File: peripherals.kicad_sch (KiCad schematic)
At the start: 1 part, among them U1 MIMX8MN5DVPIZAA

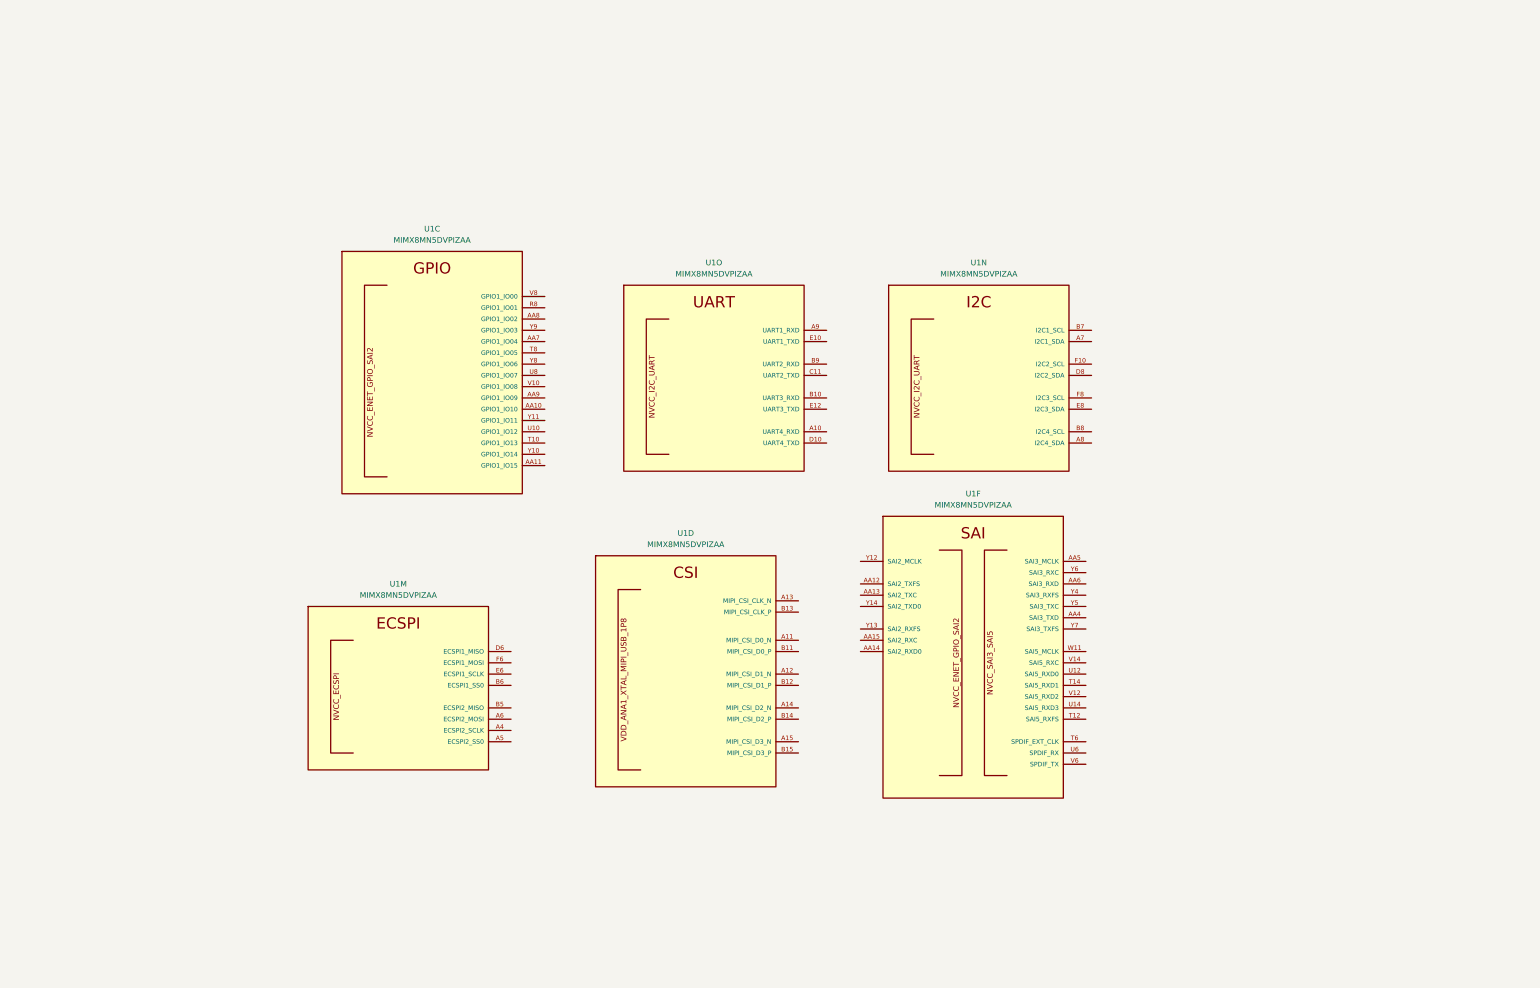
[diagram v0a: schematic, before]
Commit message: move to i.MX8M Mini
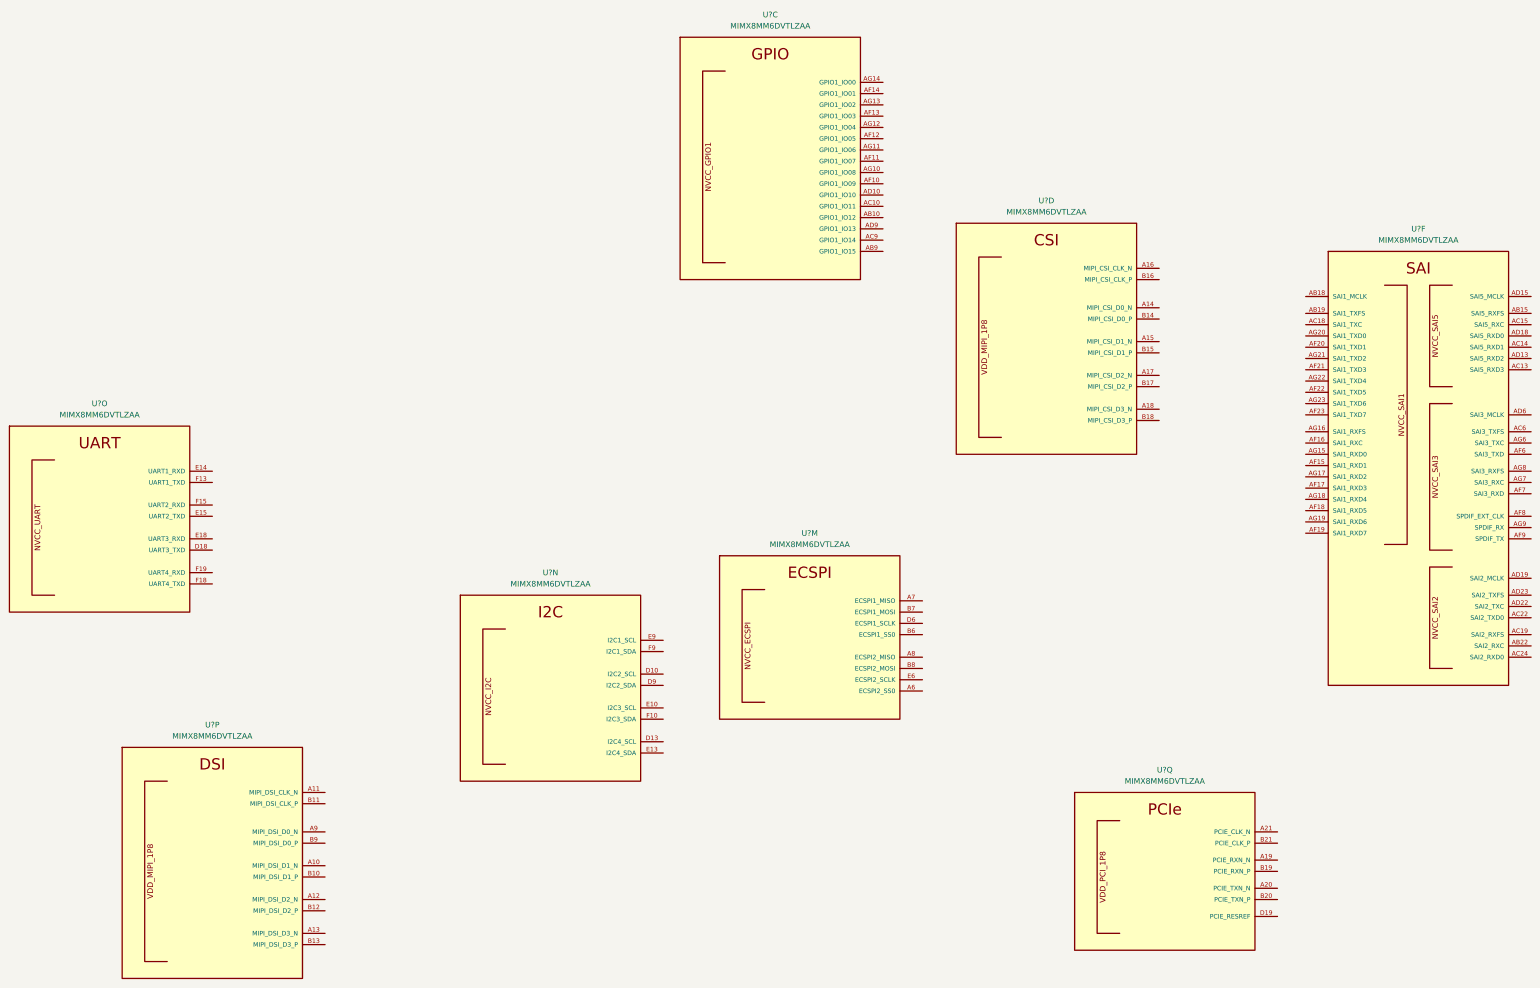
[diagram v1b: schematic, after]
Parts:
- removed U1: MIMX8MN5DVPIZAA, qsbc:SOT1967-1, symbol qsbc:MIMX8MN5DVPIZAA
- added U? (x8): MIMX8MM6DVTLZAA, qsbc:SOT1967-1, symbol qsbc:MIMX8MM6DVTLZAA

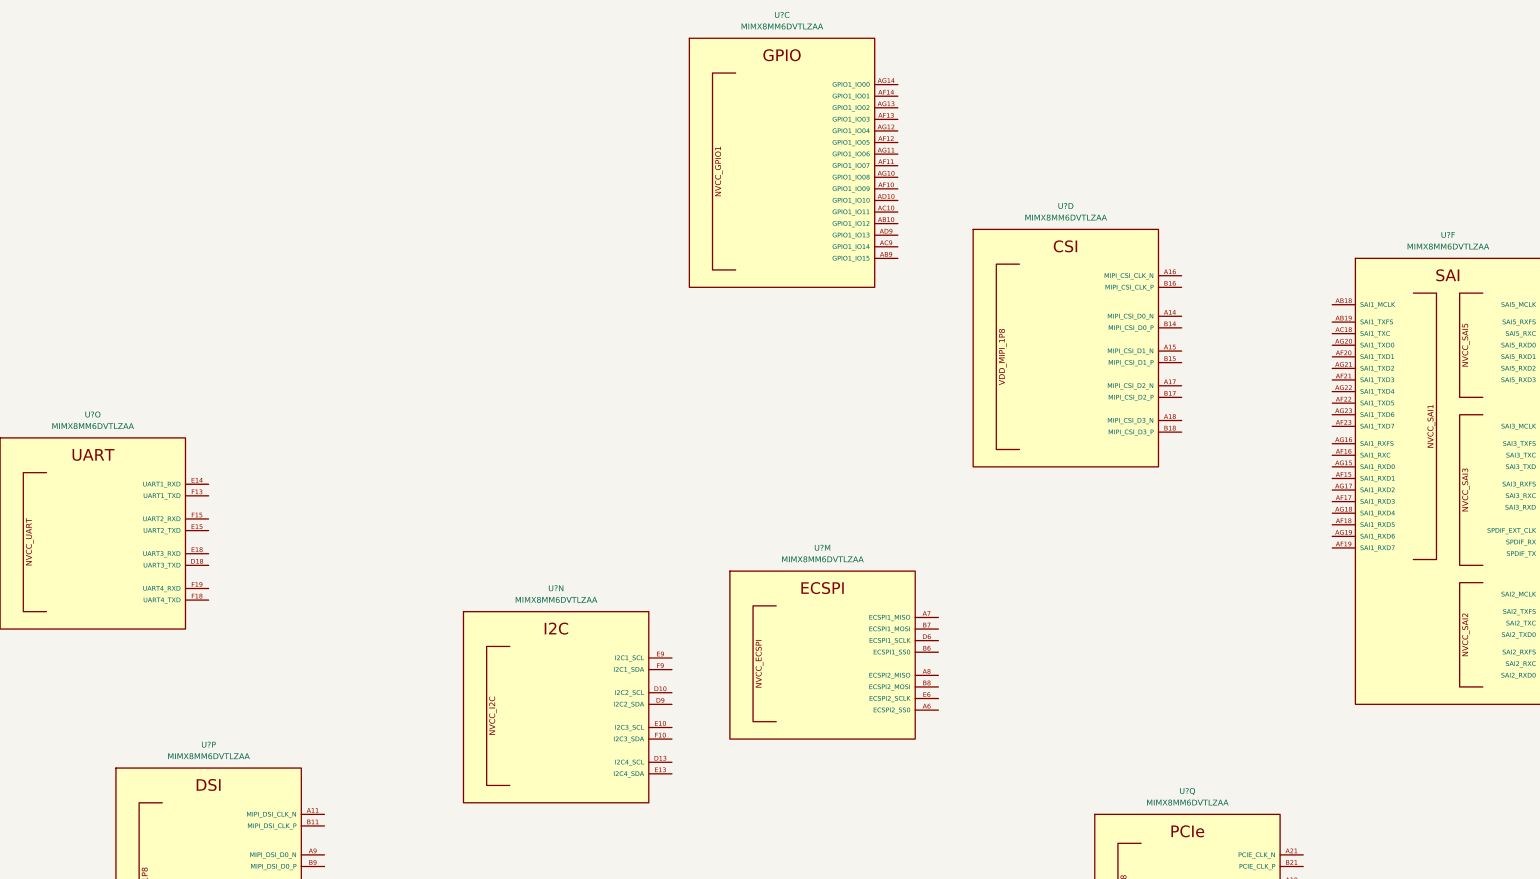
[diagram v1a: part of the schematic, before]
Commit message: ddr sch done
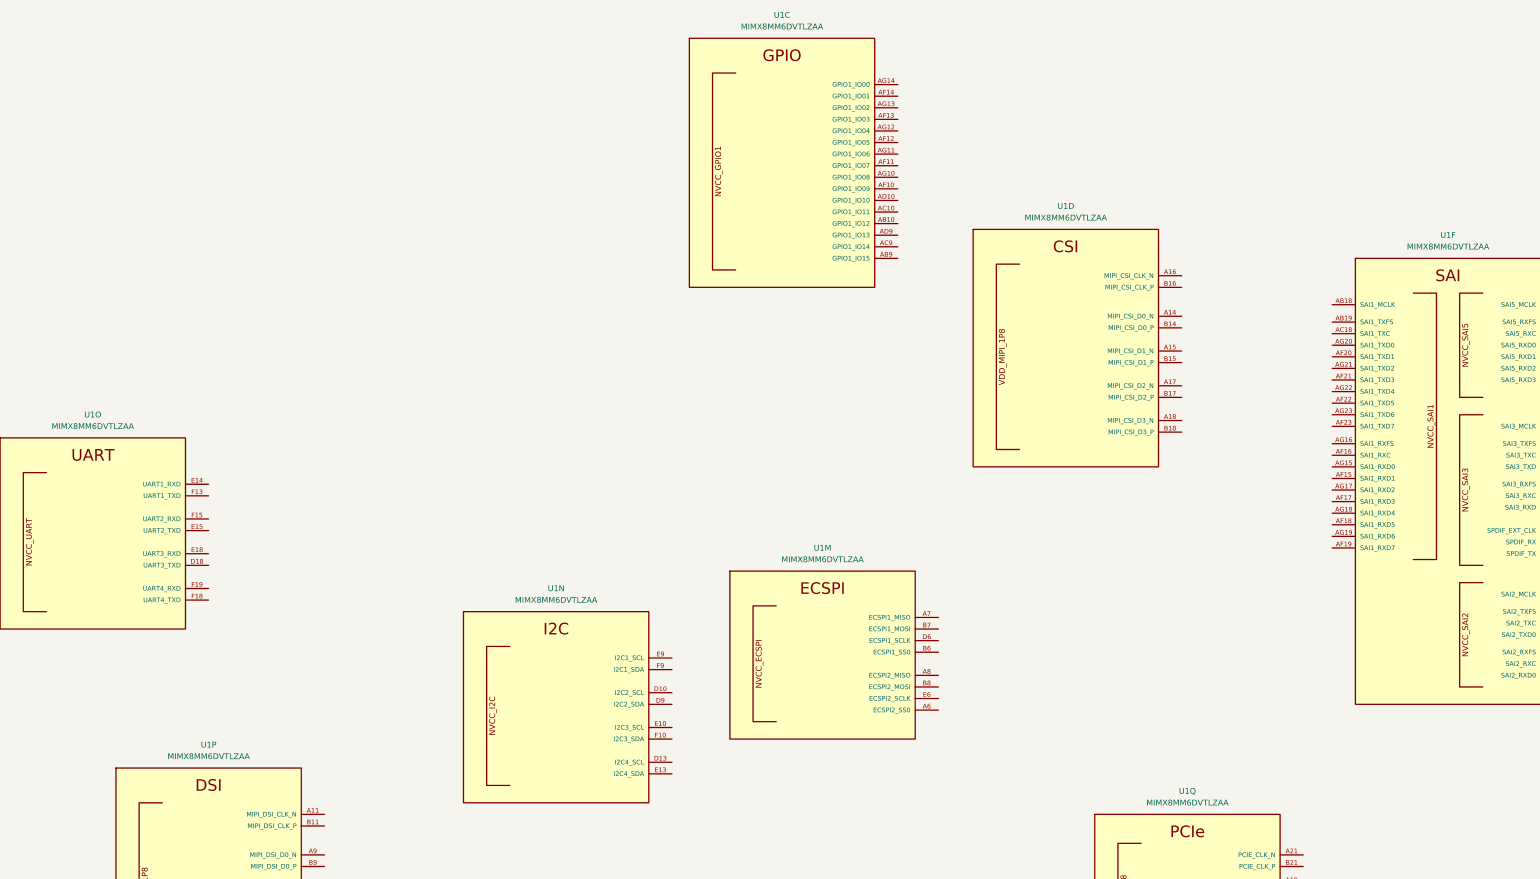
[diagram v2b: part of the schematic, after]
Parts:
- gave numbers to parts that had none: 1
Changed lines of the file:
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@@
   (symbol (lib_id "qsbc:MIMX8MM6DVTLZAA") (at 361.95 91.44 0) (unit 6)
     (in_bom yes) (on_board yes) (fields_autoplaced)
-    (property "Reference" "U?" (id 0) (at 361.95 72.39 0))
+    (property "Reference" "U1" (id 0) (at 361.95 72.39 0))
     (property "Value" "MIMX8MM6DVTLZAA" (id 1) (at 361.95 74.93 0))
     (property "Footprint" "qsbc:SOT1967-1" (id 2) (at 365.76 281.94 0)
@@
   (symbol (lib_id "qsbc:MIMX8MM6DVTLZAA") (at 224.79 160.02 0) (unit 13)
     (in_bom yes) (on_board yes) (fields_autoplaced)
-    (property "Reference" "U?" (id 0) (at 224.79 140.97 0))
+    (property "Reference" "U1" (id 0) (at 224.79 140.97 0))
     (property "Value" "MIMX8MM6DVTLZAA" (id 1) (at 224.79 143.51 0))
     (property "Footprint" "qsbc:SOT1967-1" (id 2) (at 228.6 350.52 0)
@@
   (symbol (lib_id "qsbc:MIMX8MM6DVTLZAA") (at 90.17 203.2 0) (unit 16)
     (in_bom yes) (on_board yes) (fields_autoplaced)
-    (property "Reference" "U?" (id 0) (at 90.17 184.15 0))
+    (property "Reference" "U1" (id 0) (at 90.17 184.15 0))
     (property "Value" "MIMX8MM6DVTLZAA" (id 1) (at 90.17 186.69 0))
     (property "Footprint" "qsbc:SOT1967-1" (id 2) (at 93.98 393.7 0)
@@
   (symbol (lib_id "qsbc:MIMX8MM6DVTLZAA") (at 64.77 130.81 0) (unit 15)
     (in_bom yes) (on_board yes) (fields_autoplaced)
-    (property "Reference" "U?" (id 0) (at 64.77 111.76 0))
+    (property "Reference" "U1" (id 0) (at 64.77 111.76 0))
     (property "Value" "MIMX8MM6DVTLZAA" (id 1) (at 64.77 114.3 0))
     (property "Footprint" "qsbc:SOT1967-1" (id 2) (at 68.58 321.31 0)
@@
   (symbol (lib_id "qsbc:MIMX8MM6DVTLZAA") (at 278.13 85.09 0) (unit 4)
     (in_bom yes) (on_board yes) (fields_autoplaced)
-    (property "Reference" "U?" (id 0) (at 278.13 66.04 0))
+    (property "Reference" "U1" (id 0) (at 278.13 66.04 0))
     (property "Value" "MIMX8MM6DVTLZAA" (id 1) (at 278.13 68.58 0))
     (property "Footprint" "qsbc:SOT1967-1" (id 2) (at 281.94 275.59 0)
@@
   (symbol (lib_id "qsbc:MIMX8MM6DVTLZAA") (at 215.9 43.18 0) (unit 3)
     (in_bom yes) (on_board yes) (fields_autoplaced)
-    (property "Reference" "U?" (id 0) (at 215.9 24.13 0))
+    (property "Reference" "U1" (id 0) (at 215.9 24.13 0))
     (property "Value" "MIMX8MM6DVTLZAA" (id 1) (at 215.9 26.67 0))
     (property "Footprint" "qsbc:SOT1967-1" (id 2) (at 219.71 233.68 0)
@@
   (symbol (lib_id "qsbc:MIMX8MM6DVTLZAA") (at 166.37 168.91 0) (unit 14)
     (in_bom yes) (on_board yes) (fields_autoplaced)
-    (property "Reference" "U?" (id 0) (at 166.37 149.86 0))
+    (property "Reference" "U1" (id 0) (at 166.37 149.86 0))
     (property "Value" "MIMX8MM6DVTLZAA" (id 1) (at 166.37 152.4 0))
     (property "Footprint" "qsbc:SOT1967-1" (id 2) (at 170.18 359.41 0)
@@
   (symbol (lib_id "qsbc:MIMX8MM6DVTLZAA") (at 304.8 213.36 0) (unit 17)
     (in_bom yes) (on_board yes) (fields_autoplaced)
-    (property "Reference" "U?" (id 0) (at 304.8 194.31 0))
+    (property "Reference" "U1" (id 0) (at 304.8 194.31 0))
     (property "Value" "MIMX8MM6DVTLZAA" (id 1) (at 304.8 196.85 0))
     (property "Footprint" "qsbc:SOT1967-1" (id 2) (at 308.61 403.86 0)

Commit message: misc work, usb sch done
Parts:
- removed unit 15 of U1
- removed unit 17 of U1
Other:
- moved on the sheet: U1C, U1D, U1F, U1M, U1N, U1P

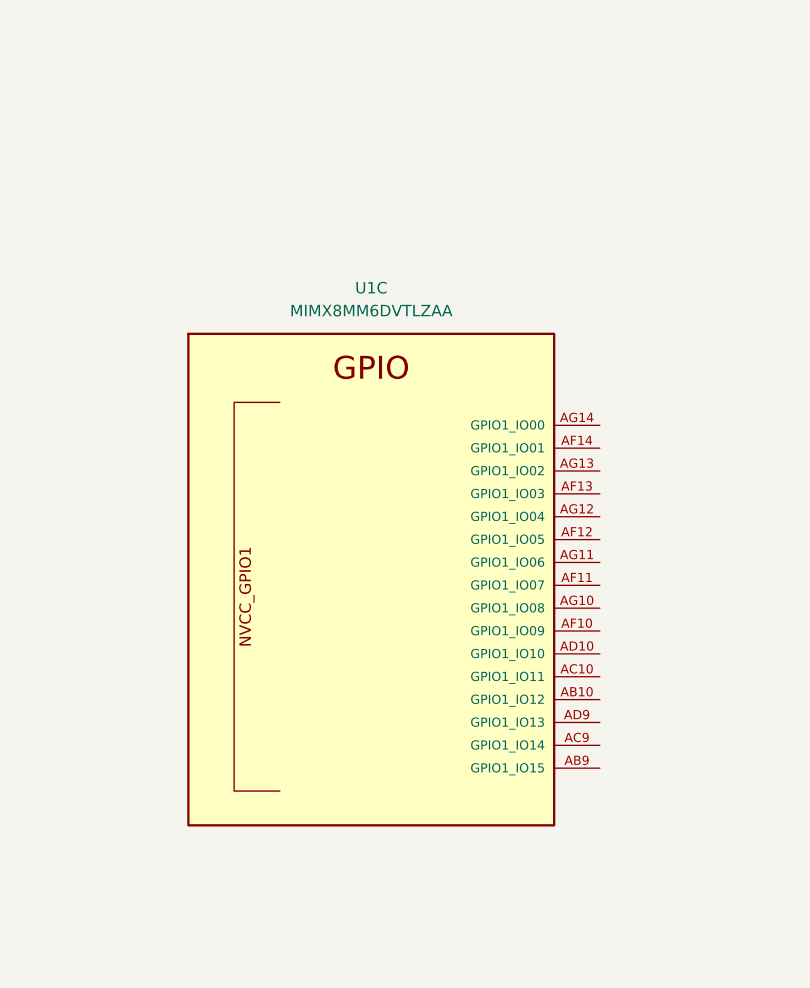
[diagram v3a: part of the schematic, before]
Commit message: enet sch done, other misc sch work
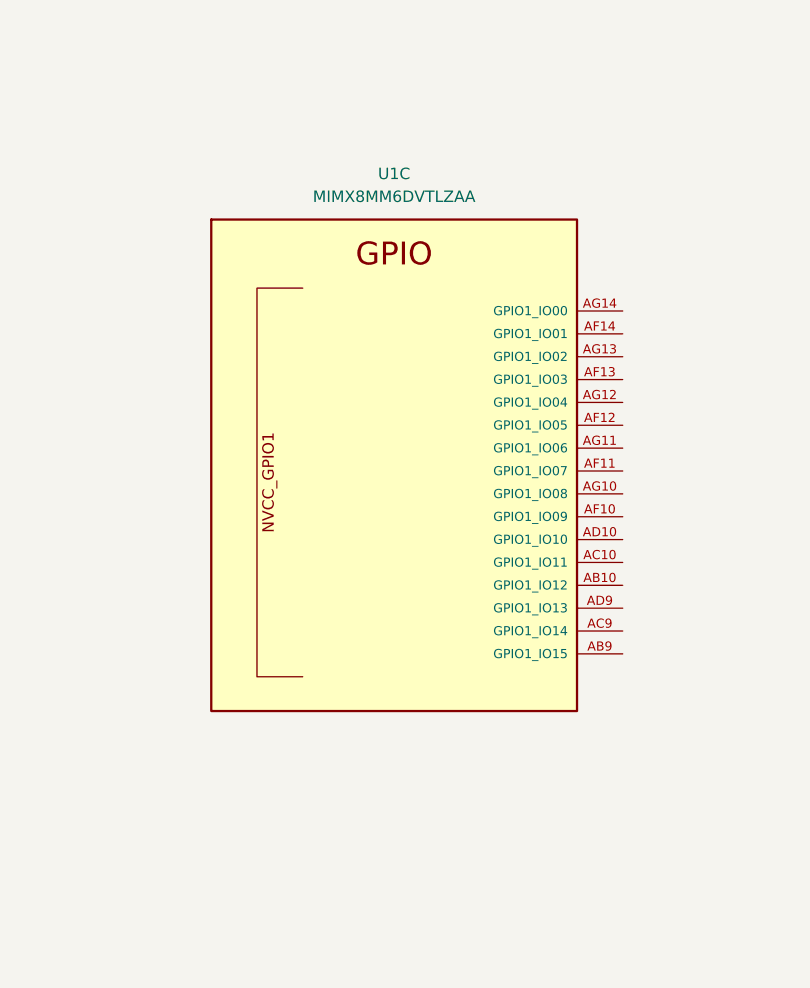
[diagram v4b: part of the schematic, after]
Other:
- moved on the sheet: U1C
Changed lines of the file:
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@@
     (pin "D19")
   )
-  (symbol (lib_id "qsbc:MIMX8MM6DVTLZAA") (at 173.99 208.28 0) (unit 3)
+  (symbol (lib_id "qsbc:MIMX8MM6DVTLZAA") (at 176.53 195.58 0) (unit 3)
     (in_bom yes) (on_board yes) (fields_autoplaced)
-    (property "Reference" "U1" (id 0) (at 173.99 189.23 0))
-    (property "Value" "MIMX8MM6DVTLZAA" (id 1) (at 173.99 191.77 0))
-    (property "Footprint" "qsbc:SOT1967-1" (id 2) (at 177.8 398.78 0)
+    (property "Reference" "U1" (id 0) (at 176.53 176.53 0))
+    (property "Value" "MIMX8MM6DVTLZAA" (id 1) (at 176.53 179.07 0))
+    (property "Footprint" "qsbc:SOT1967-1" (id 2) (at 180.34 386.08 0)
       (effects (font (size 1.27 1.27)) (justify left bottom) hide)
     )
-    (property "Datasheet" "https://www.nxp.com/docs/en/data-sheet/IMX8MMCEC.pdf" (id 3) (at 175.26 402.59 0)
+    (property "Datasheet" "https://www.nxp.com/docs/en/data-sheet/IMX8MMCEC.pdf" (id 3) (at 177.8 389.89 0)
       (effects (font (size 1.27 1.27)) (justify left bottom) hide)
     )

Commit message: storage done, peri work, misc fixes
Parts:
- added R? (x2): 4.7K, Resistor_SMD:R_0402_1005Metric, symbol Device:R
- added unit 15 of U1
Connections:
- net UART2_RTS: now reaches U1.AF7 (SAI3_RXD)
- net UART2_CTS: now reaches U1.AG7 (SAI3_RXC)
- net ~{M2_RESET}: now reaches U1.A8 (ECSPI2_MISO)
- net ~{M2_WAKE}: now reaches U1.B8 (ECSPI2_MOSI)
- net USB1_VBUS_EN: now reaches U1.AB10 (GPIO1_IO12)
- net ~{USB2_VBUS_FLT}: now reaches U1.AB9 (GPIO1_IO15)
- net ~{USB2_INT}: now reaches U1.AC10 (GPIO1_IO11)
- net USB2_VBUS_EN: now reaches U1.AC9 (GPIO1_IO14)
- net ~{USB1_INT}: now reaches U1.AD10 (GPIO1_IO10)
- net ~{USB1_VBUS_FLT}: now reaches U1.AD9 (GPIO1_IO13)
- net ~{INA_ALERT}: now reaches U1.AF10 (GPIO1_IO09)
- net ~{ENET_RESET}: now reaches U1.AF14 (GPIO1_IO01)
- net ~{WDOG}: now reaches U1.AG13 (GPIO1_IO02)
- net ~{ENET_INT}: now reaches U1.AG14 (GPIO1_IO00)
- net I2C4_SDA: now reaches U1.D13 (I2C4_SCL)
- net I2C4_SDA: now also R?.2
- net I2C4_SCL: now reaches U1.E13 (I2C4_SDA)
- net I2C4_SCL: now also R?.2
- new net UART2_RXI: U1.F15 (UART2_RXD)
- new net UART2_TXO: U1.E15 (UART2_TXD)
- new net UART4_RXI: U1.F19 (UART4_RXD)
- new net UART4_TXO: U1.F18 (UART4_TXD)
- new net VDD_1.8V: R?.1, R?.1
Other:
- moved on the sheet: U1C, U1M, U1P
